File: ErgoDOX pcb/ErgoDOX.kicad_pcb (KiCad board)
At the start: 2 copper layers, 182.8 x 158.9 mm, 77 parts, among them J1 USB, J2 3.5mm, J3 JMP, J4 JMP, SW0:10 SW0:3, SW0:11 SW0:2, SW0:12 SW0:1, SW0:7 SW0:6, SW0:8 SW0:5, SW0:9 SW0:4, SW1:10 SW1:3, SW1:11 SW1:2, SW1:12 SW1:1, SW1:13 SW1:0, SW1:9 SW1:4, SW2:10 SW2:3, SW2:11 SW2:2, SW2:12 SW2:1, SW2:13 SW2:0, SW2:7 SW2:6, SW2:8 SW2:5, SW2:9 SW2:4, SW3:10 SW3:3, SW3:11 SW3:2, SW3:12 SW3:1, SW3:13 SW3:0, SW3:8 SW3:5, SW3:9 SW3:4, SW4:10 SW4:3, SW4:11 SW4:2, SW4:12 SW4:1, SW4:13 SW4:0, SW4:7 SW4:6, SW4:8 SW4:5, SW4:9 SW4:4, SW5:10 SW5:3, SW5:11 SW5:2, SW5:12 SW5:1, SW5:13 SW5:0, SW5:7 SW5:6, SW5:8 SW5:5, SW5:9 SW5:4, U1 TEENSY2.0, U2 MCP23018

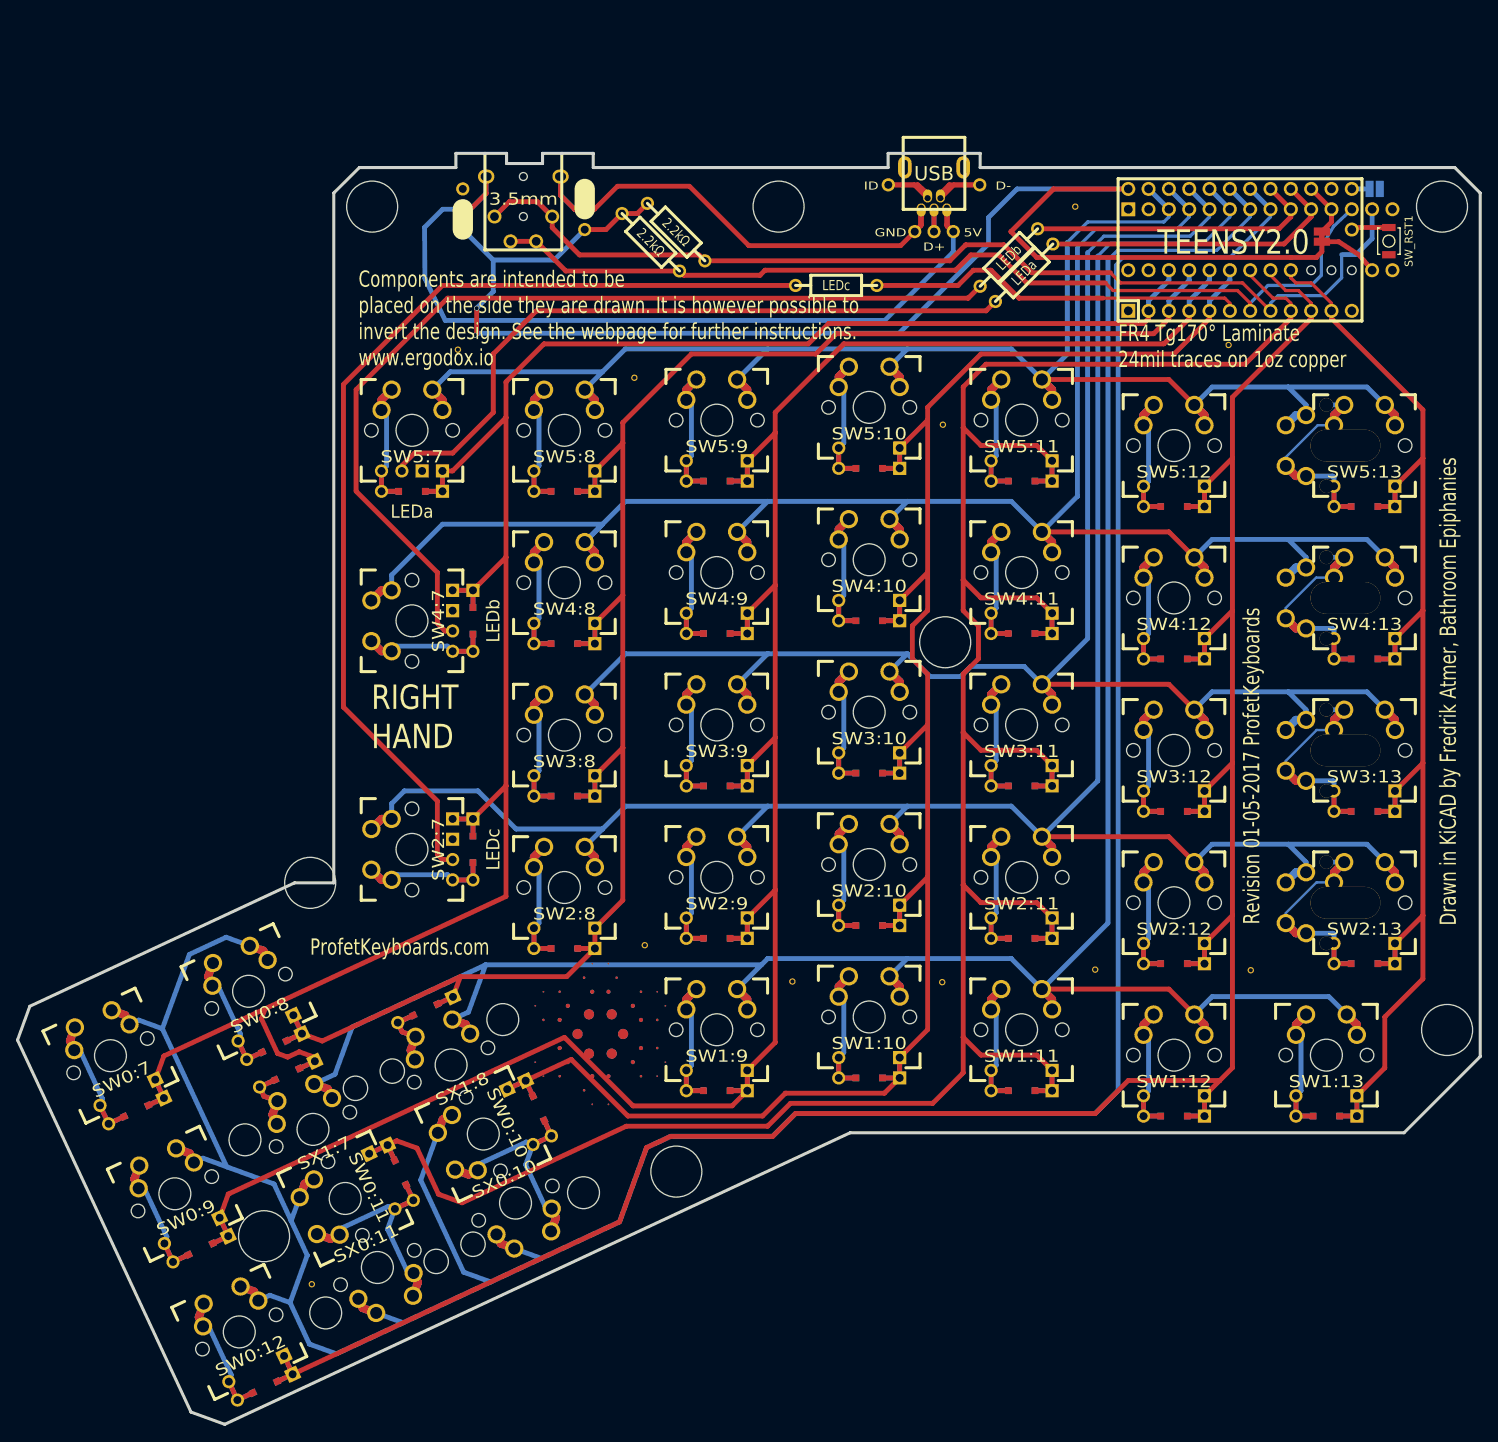
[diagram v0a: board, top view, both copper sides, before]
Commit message: Remap pins from Teensy2,0 to TinyS3
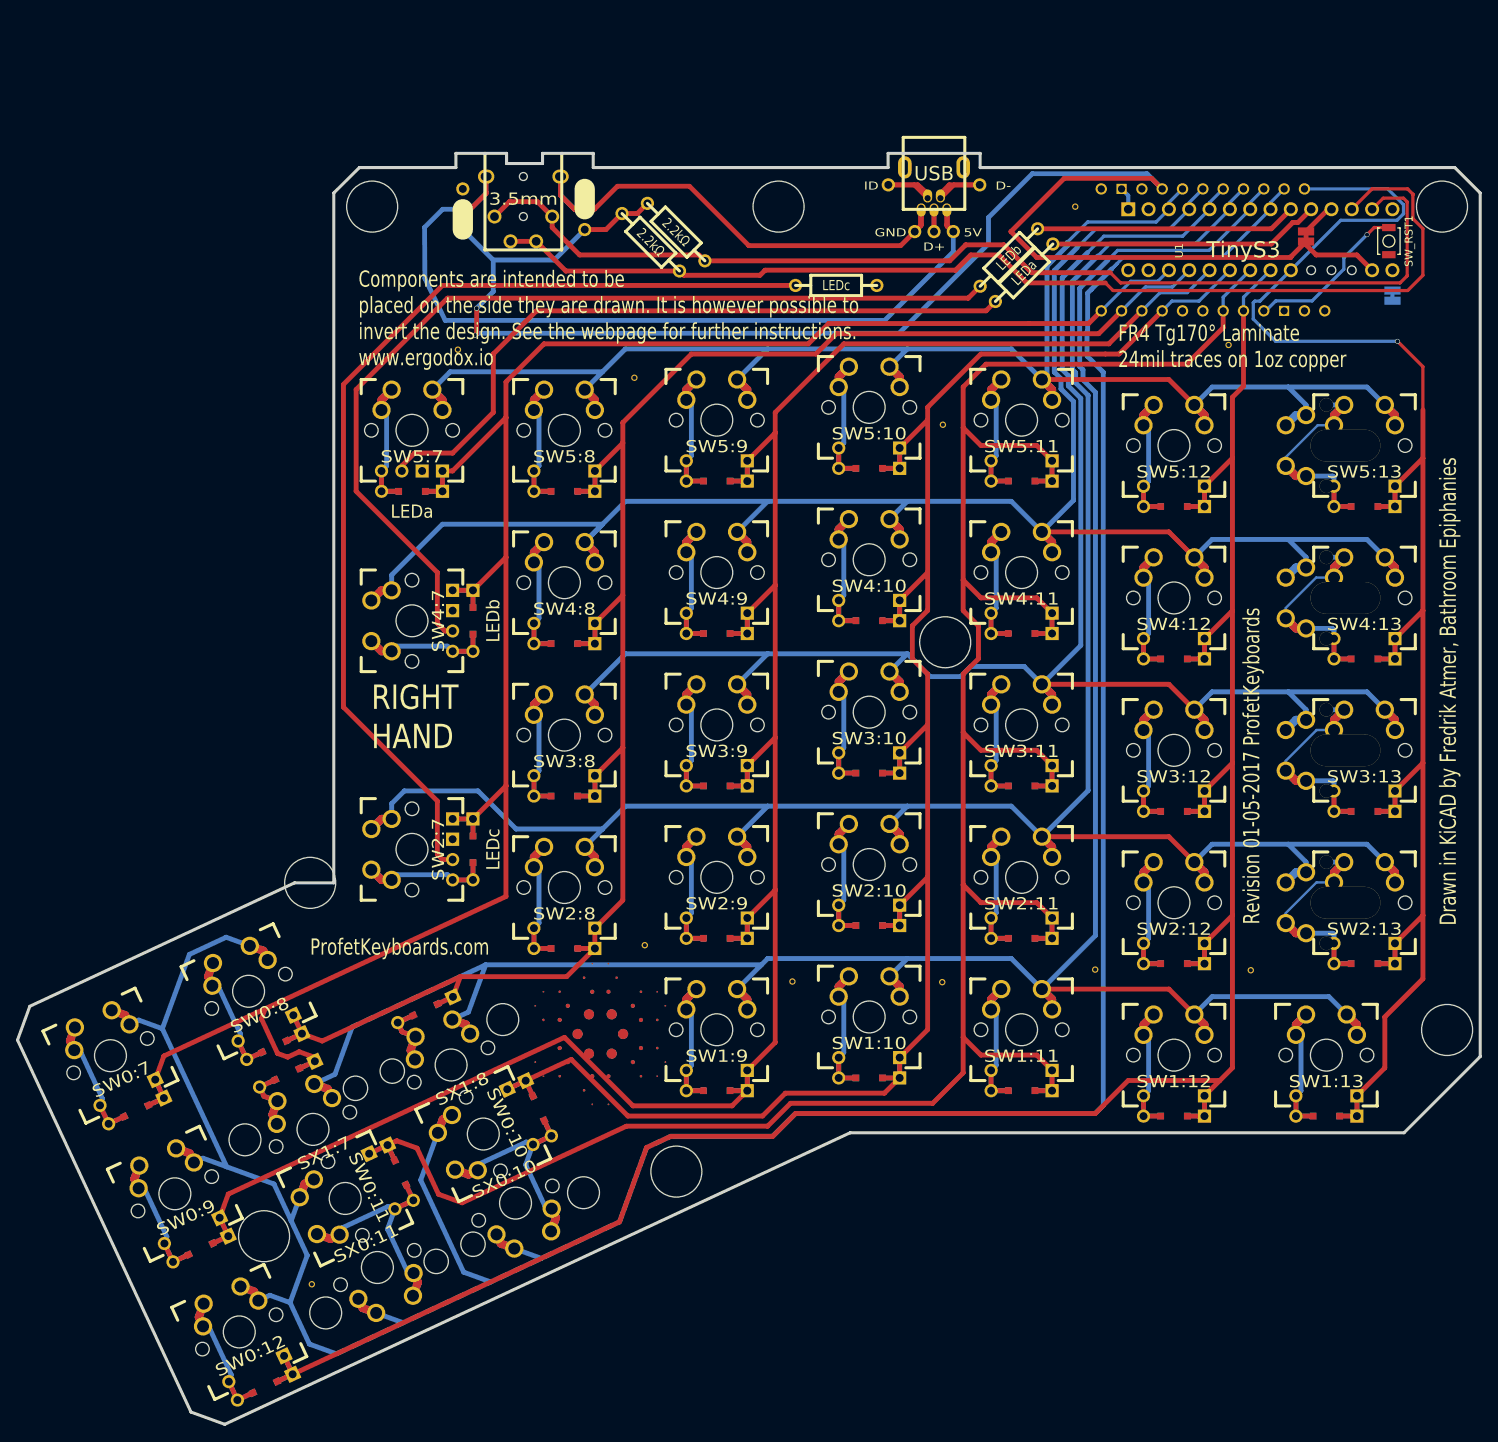
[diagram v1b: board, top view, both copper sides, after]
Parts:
- U1: value TEENSY2.0 -> TinyS3; footprint ErgoDOX pcb:TEENSY_2.0_WITH_RESET -> Espressif:TinyS3
- moved JP2 13.5 mm to (194.9, 48.3), turned to 0 degrees
- moved U1 3.41 mm to (172.5, 42.7), turned to 90 degrees
- moved JP1 1.98 mm to (184.2, 40.9)
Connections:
- net Net-(U1-Pad19) renamed /SCLS
- U1 pad 1: GND -> /VBAT
- U1 pad 10: /COL1 -> /ROW0
- U1 pad 12: Net-(U1-Pad12) -> unconnected-(U1-Pad12)
- U1 pad 16: /RST -> /COL1
- U1 pad 18: GND -> /SDAS
- U1 pad 2: /COL6 -> GND
- U1 pad 20: VCC -> /COL10
- U1 pad 21: /LED_A -> /COL4
- U1 pad 22: /LED_B -> /COL5
- U1 pad 23: /ROW0 -> /COL6
- U1 pad 3: /COL5 -> unconnected-(U1-Pad3)
- U1 pad 4: /COL4 -> VCC
- U1 pad 5: /COL10 -> /ROW5
- U1 pad 6: /LED_C -> /ROW4
- U1 pad 7: /SCLM -> /ROW3
- U1 pad 8: /SDAM -> /ROW2
- U1 pad 9: /COL11 -> /ROW1
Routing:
- net /LED_C: track 47.6 -> 0.00 mm
- net /COL0: track 159.7 -> 203.2 mm, vias 0 -> 1
- net /SCLM: track 119.7 -> 139.1 mm
- net /RST: track 4.74 -> 20.8 mm, vias 0 -> 1
- net /COL11: track 316.5 -> 307.0 mm
- net /SDAM: track 128.3 -> 136.3 mm
- net VCC: track 204.8 -> 211.7 mm
- net /ROW0: track 404.2 -> 409.9 mm
- net /COL1: track 291.8 -> 286.7 mm
- net /LED_A: track 38.2 -> 34.1 mm
- net /LED_B: track 36.8 -> 32.7 mm
- net /COL4: track 274.3 -> 272.3 mm
- net /COL10: track 233.7 -> 231.7 mm
- net /COL6: track 259.5 -> 257.5 mm
- net /COL5: track 225.8 -> 223.7 mm
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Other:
- net class Default removed

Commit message: Create preliminary layout
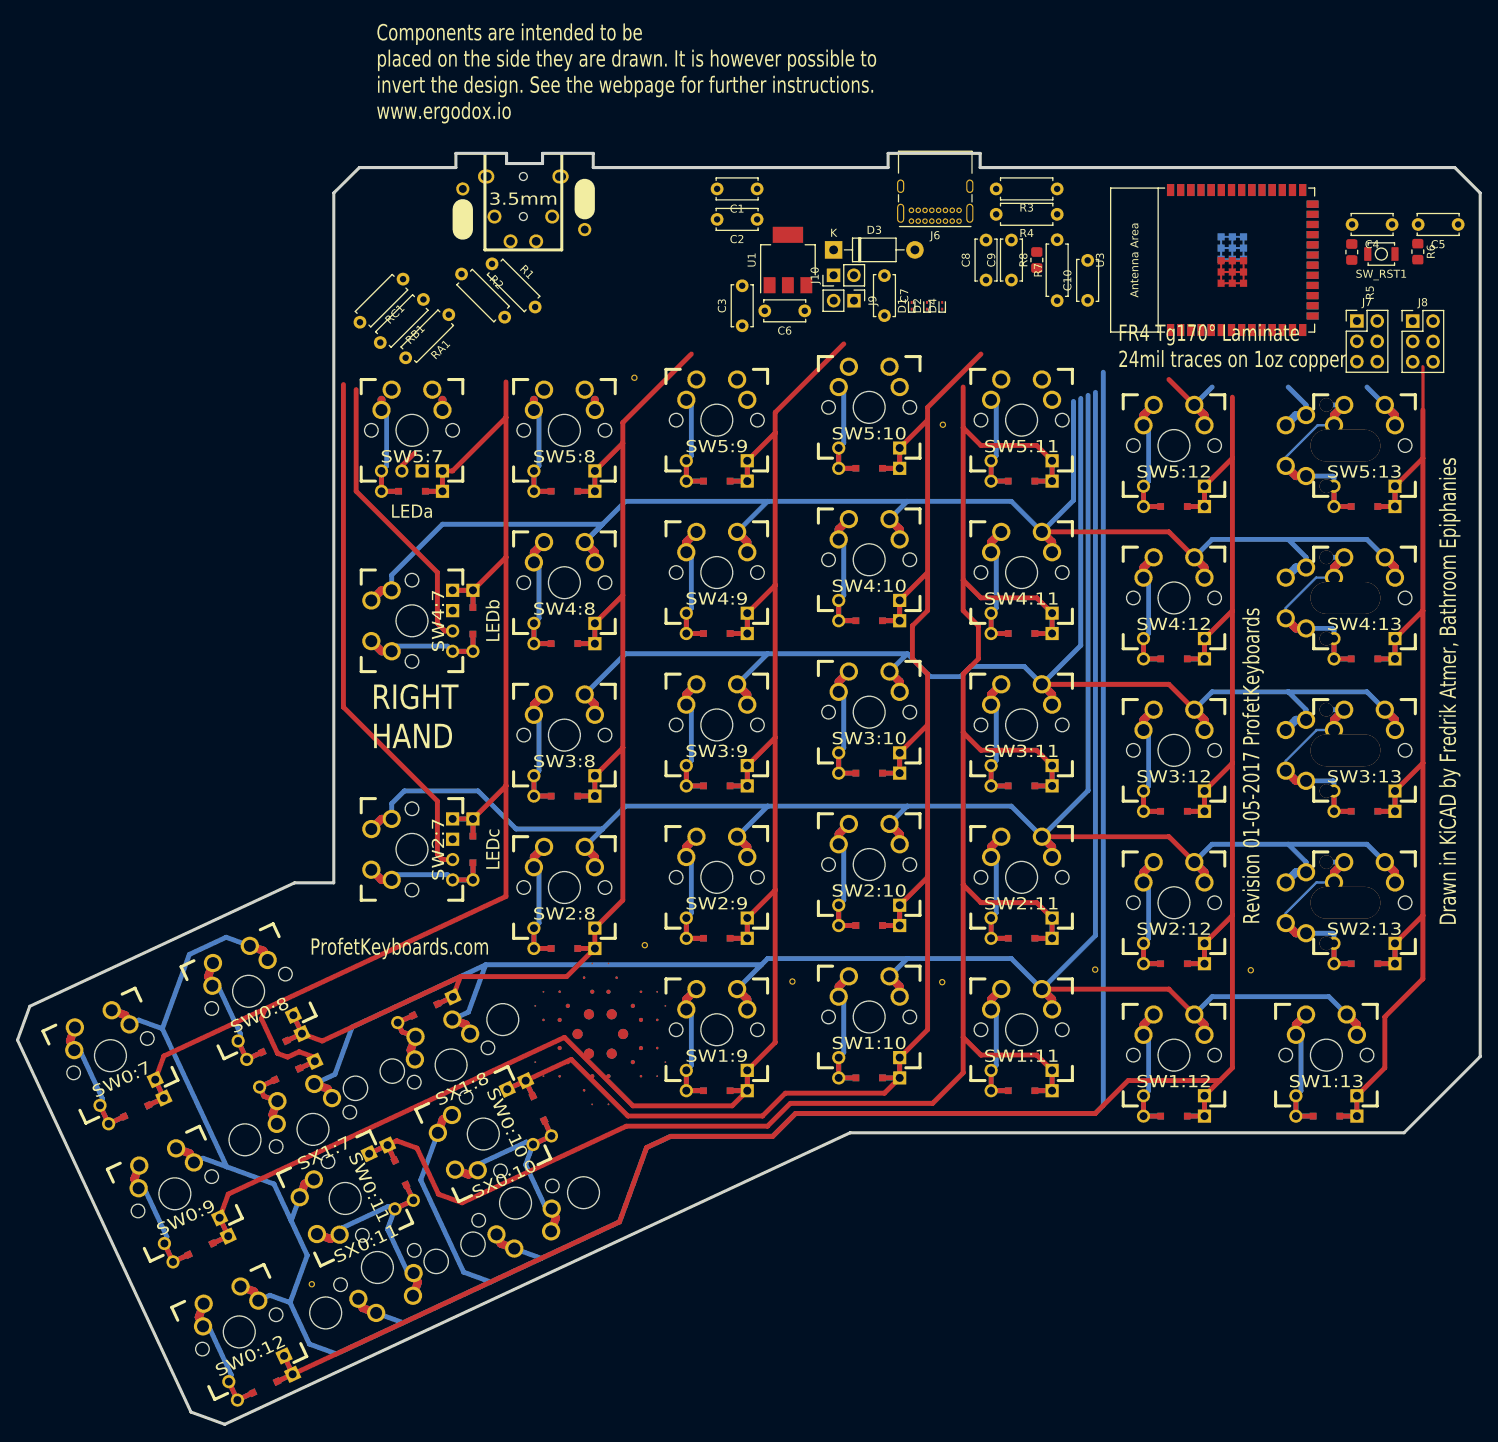
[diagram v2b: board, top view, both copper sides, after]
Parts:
- removed H99: MECHANICAL, ErgoDOXmech
- removed J1: USB, USBMINImod
- removed JP1, JP2: JUMPER, GAP
- removed the STITCHING_VIA at (78.1, 55.0)
- removed the STITCHING_VIA at (174.5, 54.4)
- removed the STITCHING_VIA at (155.3, 37.1)
- added C1: 10uF, Capacitor_THT:C_Disc_D5.0mm_W2.5mm_P5.00mm, F.Cu at (115.5, 34.9)
- added C10: 1uF, Capacitor_THT:C_Disc_D5.0mm_W2.5mm_P5.00mm, F.Cu at (156.8, 48.9)
- added C2: 0.1uF, Capacitor_THT:C_Disc_D5.0mm_W2.5mm_P5.00mm, F.Cu at (115.5, 38.7)
- added C3: 0.1uF, Capacitor_THT:C_Disc_D5.0mm_W2.5mm_P5.00mm, F.Cu at (113.7, 52.0)
- added C4: 0.1uF, Capacitor_THT:C_Disc_D5.0mm_W2.5mm_P5.00mm, F.Cu at (194.9, 39.4)
- added C5: 0.1uF, Capacitor_THT:C_Disc_D5.0mm_W2.5mm_P5.00mm, F.Cu at (203.2, 39.4)
- added C6: 10uF, Capacitor_THT:C_Disc_D5.0mm_W2.5mm_P5.00mm, F.Cu at (121.5, 50.2)
- added C7: 10uF, Capacitor_THT:C_Disc_D5.0mm_W2.5mm_P5.00mm, F.Cu at (131.4, 45.8)
- added C8: 10uF, Capacitor_THT:C_Disc_D5.0mm_W2.5mm_P5.00mm, F.Cu at (144.1, 46.3)
- added C9: 0.1uF, Capacitor_THT:C_Disc_D5.0mm_W2.5mm_P5.00mm, F.Cu at (147.3, 46.3)
- added D1: ESD9B3.3ST5G, Diode_SMD:D_SOD-923, F.Cu at (134.9, 49.5)
- added D2: ESD9B3.3ST5G, Diode_SMD:D_SOD-923, F.Cu at (136.8, 49.5)
- added D3: 1N5819, Diode_THT:D_DO-41_SOD81_P10.16mm_Horizontal, F.Cu at (125.1, 42.5)
- added D4: ESD9B3.3ST5G, Diode_SMD:D_SOD-923, F.Cu at (138.7, 49.5)
- added J10: USB VCC, Connector_PinHeader_2.54mm:PinHeader_1x02_P2.54mm_Vertical, F.Cu at (125.1, 45.7)
- added J6: USB_C_Receptacle_USB2.0, Connector_USB:USB_C_Receptacle_GCT_USB4085, F.Cu at (140.8, 39.0)
- added J7: PROG, Connector_PinHeader_2.54mm:PinHeader_2x03_P2.54mm_Vertical, F.Cu at (190.5, 51.4)
- added J8: JTAG, Connector_PinHeader_2.54mm:PinHeader_2x03_P2.54mm_Vertical, F.Cu at (197.5, 51.5)
- added J9: USB GND, Connector_PinHeader_2.54mm:PinHeader_1x02_P2.54mm_Vertical, F.Cu at (127.6, 48.9)
- added R3: 5.1k, Resistor_THT:R_Axial_DIN0207_L6.3mm_D2.5mm_P7.62mm_Horizontal, F.Cu at (153.0, 34.9)
- added R4: 5.1k, Resistor_THT:R_Axial_DIN0207_L6.3mm_D2.5mm_P7.62mm_Horizontal, F.Cu at (153.0, 38.1)
- added R5: 0, Resistor_SMD:R_0805_2012Metric_Pad1.20x1.40mm_HandSolder, F.Cu at (189.9, 42.8)
- added R6: 0, Resistor_SMD:R_0805_2012Metric_Pad1.20x1.40mm_HandSolder, F.Cu at (198.1, 42.8)
- added R7: 10k, Resistor_THT:R_Axial_DIN0207_L6.3mm_D2.5mm_P7.62mm_Horizontal, F.Cu at (153.0, 48.9)
- added R8: 0, Resistor_SMD:R_0805_2012Metric_Pad1.20x1.40mm_HandSolder, F.Cu at (150.5, 43.8)
- added U3: ESP32-S3 RH, Espressif:ESP32-S3-WROOM-1, F.Cu at (175.5, 43.8)
- R1, R2, RA1, RB1, RC1: footprint RESISTOR -> Resistor_THT:R_Axial_DIN0207_L6.3mm_D2.5mm_P7.62mm_Horizontal
- U1: value TinyS3 -> LM337_SOT223; footprint Espressif:TinyS3 -> Package_TO_SOT_SMD:SOT-223-3_TabPin2
- U2: value MCP23018 -> ESP32-S3 LH; footprint DIP28_300 -> Espressif:ESP32-S3-WROOM-1
- moved RB1 73.4 mm to (73.8, 48.7)
- moved RA1 72.1 mm to (77.0, 50.6)
- moved RC1 54.1 mm to (71.3, 46.2), turned to -135 degrees
- moved U1 53.1 mm to (119.4, 43.8)
- moved R2 24.0 mm to (78.6, 45.6)
- moved R1 23.4 mm to (82.4, 44.3)
- moved U2 3.90 mm to (175.5, 43.8), turned to -90 degrees
- moved SW_RST1 1.87 mm to (193.6, 43.1), turned to 180 degrees
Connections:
- R1 pad 2: /SDAM -> /esp_lh/SDAM
- R2 pad 2: /SCLM -> /esp_lh/SCLM
- RA1 pad 1: /LED_A -> LED_A
- RB1 pad 1: /LED_B -> LED_B
- RC1 pad 1: /LED_C -> LED_C
- U1 pad 1: /VBAT -> GND
- U1 pad 2: GND -> VCC_5V
- U1 pad 3: unconnected-(U1-Pad3) -> VCC
- U2 pad 10: /LED_A -> unconnected-(U2-Pad10)
- U2 pad 11: VCC -> unconnected-(U2-Pad11)
- U2 pad 12: /SCLM -> unconnected-(U2-Pad12)
- U2 pad 13: /SDAM -> D-
- U2 pad 14: Net-(U2-Pad14) -> D+
- U2 pad 15: GND -> unconnected-(U2-Pad15)
- U2 pad 16: VCC -> COL6
- U2 pad 2: (no net) -> /ESP_3V3
- U2 pad 20: /COL0 -> ROW0
- U2 pad 21: /COL1 -> COL5
- U2 pad 22: /COL11 -> COL4
- U2 pad 23: /COL10 -> COL10
- U2 pad 24: /COL4 -> COL11
- U2 pad 25: /COL5 -> COL1
- U2 pad 26: /COL6 -> COL0
- U2 pad 27: Net-(U2-Pad27) -> /BOOT
- U2 pad 28: Net-(U2-Pad28) -> unconnected-(U2-Pad28)
- U2 pad 3: /ROW5 -> /EN
- U2 pad 4: /ROW4 -> ROW5
- U2 pad 5: /ROW3 -> ROW4
- U2 pad 6: /ROW2 -> ROW3
- U2 pad 7: /ROW1 -> ROW2
- U2 pad 8: /ROW0 -> unconnected-(U2-Pad8)
- U2 pad 9: /LED_B -> unconnected-(U2-Pad9)
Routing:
- net VCC: track 211.7 -> 0.00 mm, vias 2 -> 0
- net /ROW5: track 224.2 -> 35.7 mm
- net /SCLM: track 139.1 -> 0.00 mm
- net /SDAM: track 136.3 -> 0.00 mm
- net Net-(J1-Pad1): track 102.6 -> 0.00 mm
- net /COL6: track 257.5 -> 168.8 mm
- net Net-(LED_A1-Pad1): track 87.6 -> 2.89 mm
- net Net-(LED_B1-Pad1): track 119.1 -> 35.7 mm
- net /COL5: track 223.7 -> 157.2 mm
- net /COL0: track 203.2 -> 139.7 mm, vias 1 -> 0
- net Net-(J1-Pad5): track 62.3 -> 0.00 mm
- net Net-(LED_C1-Pad1): track 127.4 -> 65.8 mm
- net /COL4: track 272.3 -> 222.7 mm
- net /ROW0: track 409.9 -> 363.5 mm
- net /COL11: track 307.0 -> 262.9 mm
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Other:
- board text removed: "5V"
- board text removed: "D+"
- board text removed: "D-"
- board text removed: "GND"
- board text removed: "ID"
